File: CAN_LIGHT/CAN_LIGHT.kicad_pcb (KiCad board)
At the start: 2 copper layers, 135.5 x 115.4 mm, 94 parts, among them IC1 MSPM0C1103SDDFR, J1 Conn_ARM_SWD_TagConnect_TC2030

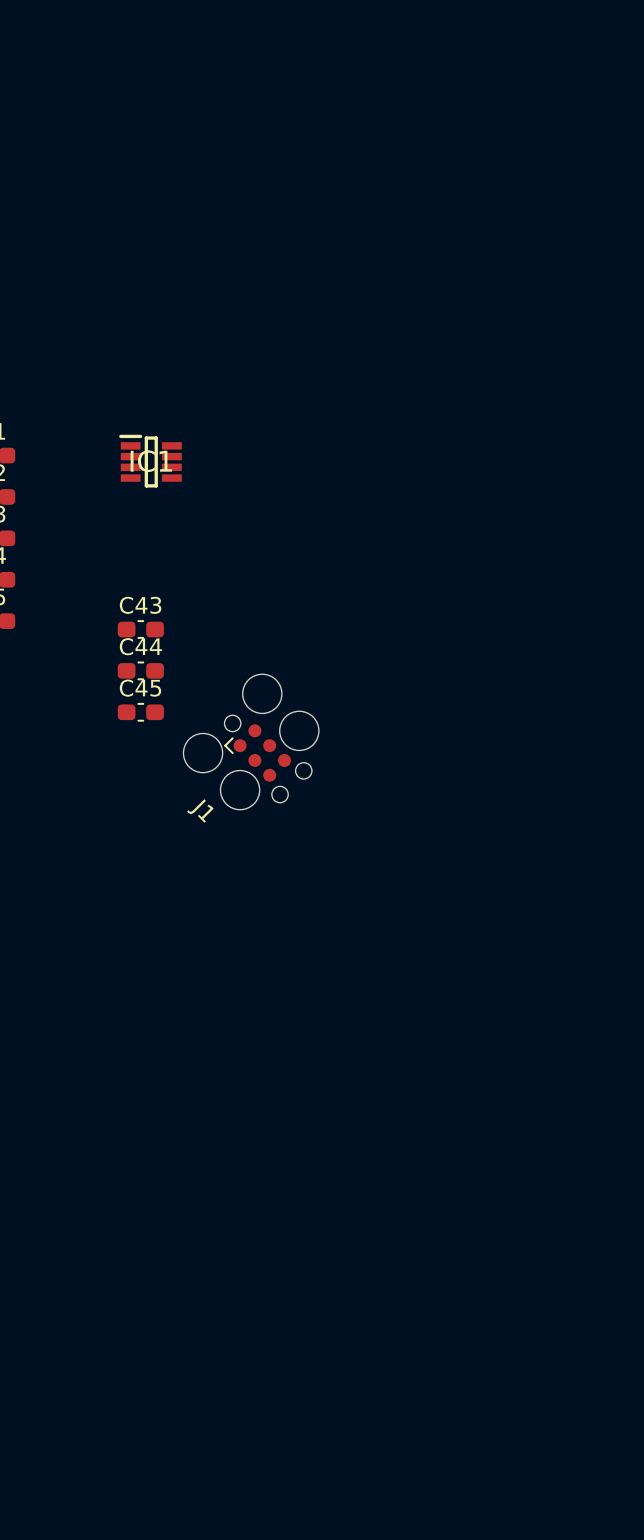
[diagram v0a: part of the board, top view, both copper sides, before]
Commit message: Export initial STEP file to print
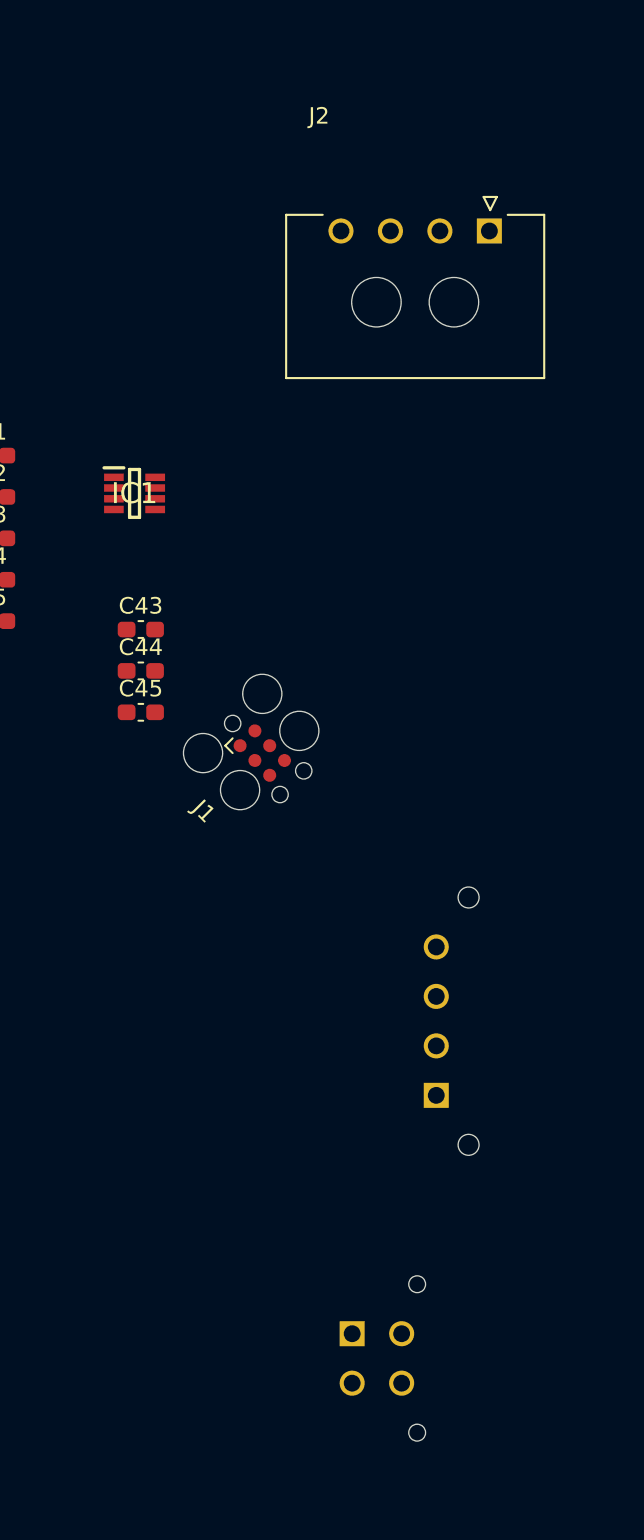
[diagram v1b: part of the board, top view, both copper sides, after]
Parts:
- added J2: 436500401, 436500401:MOLEX_436500401, F.Cu at (55.6, 42.4)
- added J3: 436500428, 436500428:CON_436500428_MOL, B.Cu at (52.3, 94.8)
- added J4: 430450428, 430450428:CON_430450428_MOL, B.Cu at (47.2, 109.3)
- moved IC1 2.16 mm to (34.0, 58.3)

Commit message: Add back side LEDs
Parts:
- removed IC1: MSPM0C1103SDDFR, MSPM0C1103SDDFR:SOT65P280X110-8N
- removed J4: 430450428, 430450428:CON_430450428_MOL
- added C46: 0.1uF, Capacitor_SMD:C_0603_1608Metric_Pad1.08x0.95mm_HandSolder, B.Cu at (230.2, 27.2)
- added C47: 0.1uF, Capacitor_SMD:C_0603_1608Metric_Pad1.08x0.95mm_HandSolder, B.Cu at (230.2, 29.7)
- added C48: 0.1uF, Capacitor_SMD:C_0603_1608Metric_Pad1.08x0.95mm_HandSolder, B.Cu at (230.2, 32.2)
- added C49: 0.1uF, Capacitor_SMD:C_0603_1608Metric_Pad1.08x0.95mm_HandSolder, B.Cu at (230.2, 34.7)
- added C50: 0.1uF, Capacitor_SMD:C_0603_1608Metric_Pad1.08x0.95mm_HandSolder, B.Cu at (230.2, 37.2)
- added C51: 0.1uF, Capacitor_SMD:C_0603_1608Metric_Pad1.08x0.95mm_HandSolder, B.Cu at (230.2, 39.7)
- added C52: 0.1uF, Capacitor_SMD:C_0603_1608Metric_Pad1.08x0.95mm_HandSolder, B.Cu at (230.2, 42.2)
- added C53: 0.1uF, Capacitor_SMD:C_0603_1608Metric_Pad1.08x0.95mm_HandSolder, B.Cu at (230.2, 44.7)
- added C54: 0.1uF, Capacitor_SMD:C_0603_1608Metric_Pad1.08x0.95mm_HandSolder, B.Cu at (230.2, 47.2)
- added C55: 0.1uF, Capacitor_SMD:C_0603_1608Metric_Pad1.08x0.95mm_HandSolder, B.Cu at (225.9, 27.2)
- added C56: 0.1uF, Capacitor_SMD:C_0603_1608Metric_Pad1.08x0.95mm_HandSolder, B.Cu at (225.9, 29.7)
- added C57: 0.1uF, Capacitor_SMD:C_0603_1608Metric_Pad1.08x0.95mm_HandSolder, B.Cu at (225.9, 32.2)
- added C58: 0.1uF, Capacitor_SMD:C_0603_1608Metric_Pad1.08x0.95mm_HandSolder, B.Cu at (225.9, 34.7)
- added C59: 0.1uF, Capacitor_SMD:C_0603_1608Metric_Pad1.08x0.95mm_HandSolder, B.Cu at (225.9, 37.2)
- added C60: 0.1uF, Capacitor_SMD:C_0603_1608Metric_Pad1.08x0.95mm_HandSolder, B.Cu at (225.9, 39.7)
- added C61: 0.1uF, Capacitor_SMD:C_0603_1608Metric_Pad1.08x0.95mm_HandSolder, B.Cu at (225.9, 42.2)
- added C62: 0.1uF, Capacitor_SMD:C_0603_1608Metric_Pad1.08x0.95mm_HandSolder, B.Cu at (225.9, 44.7)
- added C63: 0.1uF, Capacitor_SMD:C_0603_1608Metric_Pad1.08x0.95mm_HandSolder, B.Cu at (225.9, 47.2)
- added C64: 0.1uF, Capacitor_SMD:C_0603_1608Metric_Pad1.08x0.95mm_HandSolder, B.Cu at (221.5, 27.2)
- added C65: 0.1uF, Capacitor_SMD:C_0603_1608Metric_Pad1.08x0.95mm_HandSolder, B.Cu at (221.5, 29.7)
- added C66: 0.1uF, Capacitor_SMD:C_0603_1608Metric_Pad1.08x0.95mm_HandSolder, B.Cu at (221.5, 32.2)
- added C67: 0.1uF, Capacitor_SMD:C_0603_1608Metric_Pad1.08x0.95mm_HandSolder, B.Cu at (221.5, 34.7)
- added C68: 0.1uF, Capacitor_SMD:C_0603_1608Metric_Pad1.08x0.95mm_HandSolder, B.Cu at (221.5, 37.2)
- added C69: 0.1uF, Capacitor_SMD:C_0603_1608Metric_Pad1.08x0.95mm_HandSolder, B.Cu at (221.5, 39.7)
- added C70: 0.1uF, Capacitor_SMD:C_0603_1608Metric_Pad1.08x0.95mm_HandSolder, B.Cu at (221.5, 42.2)
- added C71: 0.1uF, Capacitor_SMD:C_0603_1608Metric_Pad1.08x0.95mm_HandSolder, B.Cu at (221.5, 44.7)
- added C72: 0.1uF, Capacitor_SMD:C_0603_1608Metric_Pad1.08x0.95mm_HandSolder, B.Cu at (221.5, 47.2)
- added C73: 0.1uF, Capacitor_SMD:C_0603_1608Metric_Pad1.08x0.95mm_HandSolder, B.Cu at (217.2, 27.2)
- added C74: 0.1uF, Capacitor_SMD:C_0603_1608Metric_Pad1.08x0.95mm_HandSolder, B.Cu at (217.2, 29.7)
- added C75: 0.1uF, Capacitor_SMD:C_0603_1608Metric_Pad1.08x0.95mm_HandSolder, B.Cu at (217.2, 32.2)
- added C76: 0.1uF, Capacitor_SMD:C_0603_1608Metric_Pad1.08x0.95mm_HandSolder, B.Cu at (217.2, 34.7)
- added C77: 0.1uF, Capacitor_SMD:C_0603_1608Metric_Pad1.08x0.95mm_HandSolder, B.Cu at (217.2, 37.2)
- added C78: 0.1uF, Capacitor_SMD:C_0603_1608Metric_Pad1.08x0.95mm_HandSolder, B.Cu at (217.2, 39.7)
- added C79: 0.1uF, Capacitor_SMD:C_0603_1608Metric_Pad1.08x0.95mm_HandSolder, B.Cu at (217.2, 42.2)
- added C80: 0.1uF, Capacitor_SMD:C_0603_1608Metric_Pad1.08x0.95mm_HandSolder, B.Cu at (217.2, 44.7)
- added C81: 0.1uF, Capacitor_SMD:C_0603_1608Metric_Pad1.08x0.95mm_HandSolder, B.Cu at (217.2, 47.2)
- added C82: 0.1uF, Capacitor_SMD:C_0603_1608Metric_Pad1.08x0.95mm_HandSolder, B.Cu at (212.8, 27.2)
- added C83: 0.1uF, Capacitor_SMD:C_0603_1608Metric_Pad1.08x0.95mm_HandSolder, B.Cu at (212.8, 29.7)
- added C84: 0.1uF, Capacitor_SMD:C_0603_1608Metric_Pad1.08x0.95mm_HandSolder, B.Cu at (212.8, 32.2)
- added C85: 0.1uF, Capacitor_SMD:C_0603_1608Metric_Pad1.08x0.95mm_HandSolder, B.Cu at (212.8, 34.7)
- added C86: 0.1uF, Capacitor_SMD:C_0603_1608Metric_Pad1.08x0.95mm_HandSolder, B.Cu at (212.8, 37.2)
- added C87: 0.1uF, Capacitor_SMD:C_0603_1608Metric_Pad1.08x0.95mm_HandSolder, B.Cu at (212.8, 39.7)
- added D43: ~, IN-PI4818QAS5R5G5BPW:INPI4818QAS5R5G5BPW, B.Cu at (270.6, 28.5)
- added D44: ~, IN-PI4818QAS5R5G5BPW:INPI4818QAS5R5G5BPW, B.Cu at (270.6, 33.4)
- added D45: ~, IN-PI4818QAS5R5G5BPW:INPI4818QAS5R5G5BPW, B.Cu at (270.6, 38.3)
- added D46: ~, IN-PI4818QAS5R5G5BPW:INPI4818QAS5R5G5BPW, B.Cu at (270.6, 43.2)
- added D47: ~, IN-PI4818QAS5R5G5BPW:INPI4818QAS5R5G5BPW, B.Cu at (270.6, 48.1)
- added D48: ~, IN-PI4818QAS5R5G5BPW:INPI4818QAS5R5G5BPW, B.Cu at (270.6, 53.0)
- added D49: ~, IN-PI4818QAS5R5G5BPW:INPI4818QAS5R5G5BPW, B.Cu at (270.6, 57.9)
- added D50: ~, IN-PI4818QAS5R5G5BPW:INPI4818QAS5R5G5BPW, B.Cu at (270.6, 62.8)
- added D51: ~, IN-PI4818QAS5R5G5BPW:INPI4818QAS5R5G5BPW, B.Cu at (270.6, 67.7)
- added D52: ~, IN-PI4818QAS5R5G5BPW:INPI4818QAS5R5G5BPW, B.Cu at (262.1, 28.5)
- added D53: ~, IN-PI4818QAS5R5G5BPW:INPI4818QAS5R5G5BPW, B.Cu at (262.1, 33.4)
- added D54: ~, IN-PI4818QAS5R5G5BPW:INPI4818QAS5R5G5BPW, B.Cu at (262.1, 38.3)
- added D55: ~, IN-PI4818QAS5R5G5BPW:INPI4818QAS5R5G5BPW, B.Cu at (262.1, 43.2)
- added D56: ~, IN-PI4818QAS5R5G5BPW:INPI4818QAS5R5G5BPW, B.Cu at (262.1, 48.1)
- added D57: ~, IN-PI4818QAS5R5G5BPW:INPI4818QAS5R5G5BPW, B.Cu at (262.1, 53.0)
- added D58: ~, IN-PI4818QAS5R5G5BPW:INPI4818QAS5R5G5BPW, B.Cu at (262.1, 57.9)
- added D59: ~, IN-PI4818QAS5R5G5BPW:INPI4818QAS5R5G5BPW, B.Cu at (262.1, 62.8)
- added D60: ~, IN-PI4818QAS5R5G5BPW:INPI4818QAS5R5G5BPW, B.Cu at (262.1, 67.7)
- added D61: ~, IN-PI4818QAS5R5G5BPW:INPI4818QAS5R5G5BPW, B.Cu at (253.6, 28.5)
- added D62: ~, IN-PI4818QAS5R5G5BPW:INPI4818QAS5R5G5BPW, B.Cu at (253.6, 33.4)
- added D63: ~, IN-PI4818QAS5R5G5BPW:INPI4818QAS5R5G5BPW, B.Cu at (253.6, 38.3)
- added D64: ~, IN-PI4818QAS5R5G5BPW:INPI4818QAS5R5G5BPW, B.Cu at (253.6, 43.2)
- added D65: ~, IN-PI4818QAS5R5G5BPW:INPI4818QAS5R5G5BPW, B.Cu at (253.6, 48.1)
- added D66: ~, IN-PI4818QAS5R5G5BPW:INPI4818QAS5R5G5BPW, B.Cu at (253.6, 53.0)
- added D67: ~, IN-PI4818QAS5R5G5BPW:INPI4818QAS5R5G5BPW, B.Cu at (253.6, 57.9)
- added D68: ~, IN-PI4818QAS5R5G5BPW:INPI4818QAS5R5G5BPW, B.Cu at (253.6, 62.8)
- added D69: ~, IN-PI4818QAS5R5G5BPW:INPI4818QAS5R5G5BPW, B.Cu at (253.6, 67.7)
- added D70: ~, IN-PI4818QAS5R5G5BPW:INPI4818QAS5R5G5BPW, B.Cu at (245.1, 28.5)
- added D71: ~, IN-PI4818QAS5R5G5BPW:INPI4818QAS5R5G5BPW, B.Cu at (245.1, 33.4)
- added D72: ~, IN-PI4818QAS5R5G5BPW:INPI4818QAS5R5G5BPW, B.Cu at (245.1, 38.3)
- added D73: ~, IN-PI4818QAS5R5G5BPW:INPI4818QAS5R5G5BPW, B.Cu at (245.1, 43.2)
- added D74: ~, IN-PI4818QAS5R5G5BPW:INPI4818QAS5R5G5BPW, B.Cu at (245.1, 48.1)
- added D75: ~, IN-PI4818QAS5R5G5BPW:INPI4818QAS5R5G5BPW, B.Cu at (245.1, 53.0)
- added D76: ~, IN-PI4818QAS5R5G5BPW:INPI4818QAS5R5G5BPW, B.Cu at (245.1, 57.9)
- added D77: ~, IN-PI4818QAS5R5G5BPW:INPI4818QAS5R5G5BPW, B.Cu at (245.1, 62.8)
- added D78: ~, IN-PI4818QAS5R5G5BPW:INPI4818QAS5R5G5BPW, B.Cu at (245.1, 67.7)
- added D79: ~, IN-PI4818QAS5R5G5BPW:INPI4818QAS5R5G5BPW, B.Cu at (236.6, 28.5)
- added D80: ~, IN-PI4818QAS5R5G5BPW:INPI4818QAS5R5G5BPW, B.Cu at (236.6, 33.4)
- added D81: ~, IN-PI4818QAS5R5G5BPW:INPI4818QAS5R5G5BPW, B.Cu at (236.6, 38.3)
- added D82: ~, IN-PI4818QAS5R5G5BPW:INPI4818QAS5R5G5BPW, B.Cu at (236.6, 43.2)
- added D83: ~, IN-PI4818QAS5R5G5BPW:INPI4818QAS5R5G5BPW, B.Cu at (236.6, 48.1)
- added D84: ~, IN-PI4818QAS5R5G5BPW:INPI4818QAS5R5G5BPW, B.Cu at (236.6, 53.0)
- added U1: MSPM0C1103SDDFR, MSPM0C1103SDDFR:SOT65P280X110-8N, B.Cu at (229.8, 50.7)
- J2: value 436500401 -> 436500428; footprint 436500401:MOLEX_436500401 -> 436500428:CON_436500428_MOL
- J3: value 436500428 -> 430450428; footprint 436500428:CON_436500428_MOL -> 430450428:CON_430450428_MOL
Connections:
- D42 pad 3: unconnected-(D42-DOUT-Pad3) -> Net-(D42-DOUT)

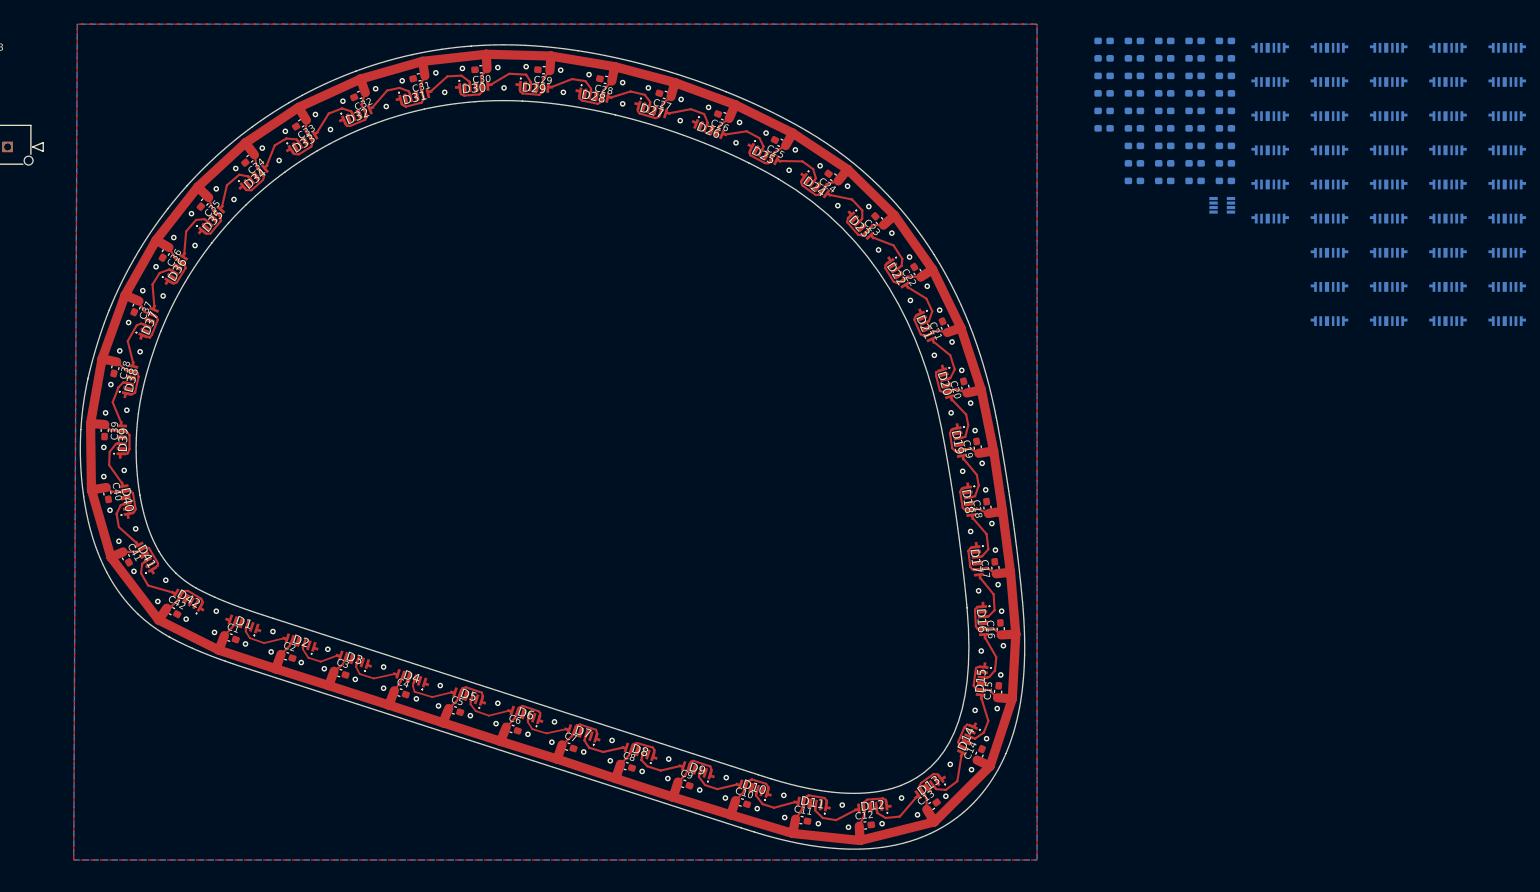
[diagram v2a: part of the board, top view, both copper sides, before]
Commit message: Roughly place backside LEDs
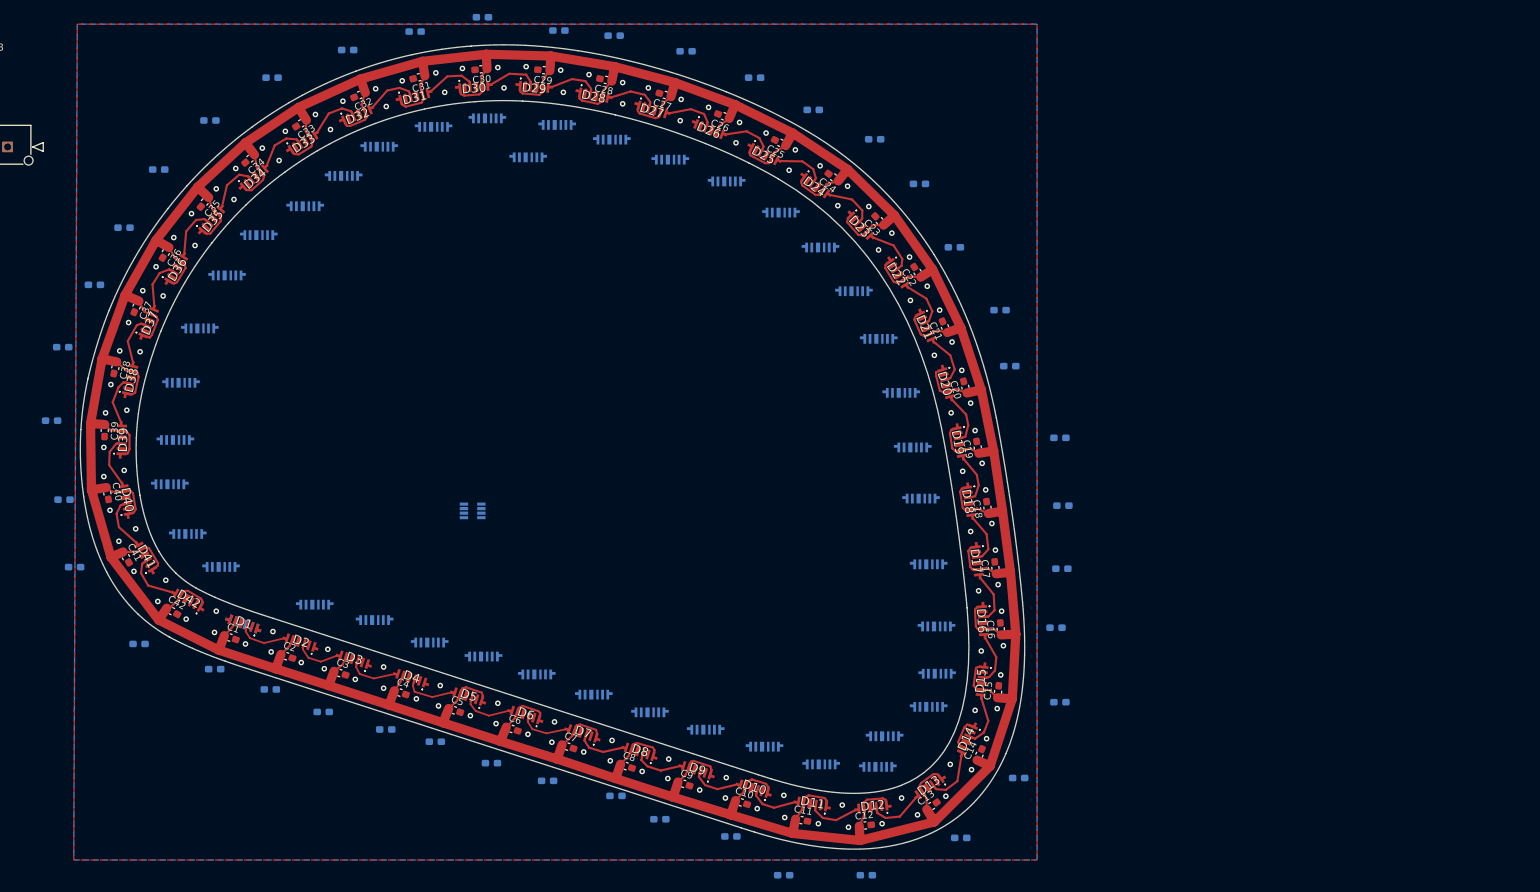
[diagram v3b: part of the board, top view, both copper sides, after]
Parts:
- moved D43 198.9 mm to (89.5, 110.5), turned to -19 degrees
- moved D44 186.8 mm to (99.6, 108.3)
- moved D45 177.8 mm to (108.2, 110.5)
- moved C46 170.7 mm to (85.2, 117.3), turned to 0 degrees
- moved D46 169.9 mm to (116.1, 113.8)
- moved D82 164.9 mm to (78.8, 91.1)
- moved C47 164.2 mm to (93.2, 120.2)
- moved D81 163.8 mm to (79.6, 84.7)
- moved D83 163.2 mm to (81.4, 98.2)
- moved D80 162.1 mm to (80.4, 76.5)
- moved D47 161.7 mm to (123.8, 115.8)
- moved C86 161.5 mm to (65.2, 102.6)
- moved C85 160.2 mm to (63.6, 93.0)
- moved C84 158.9 mm to (61.8, 81.6)
- moved D79 158.7 mm to (83.1, 68.7)
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
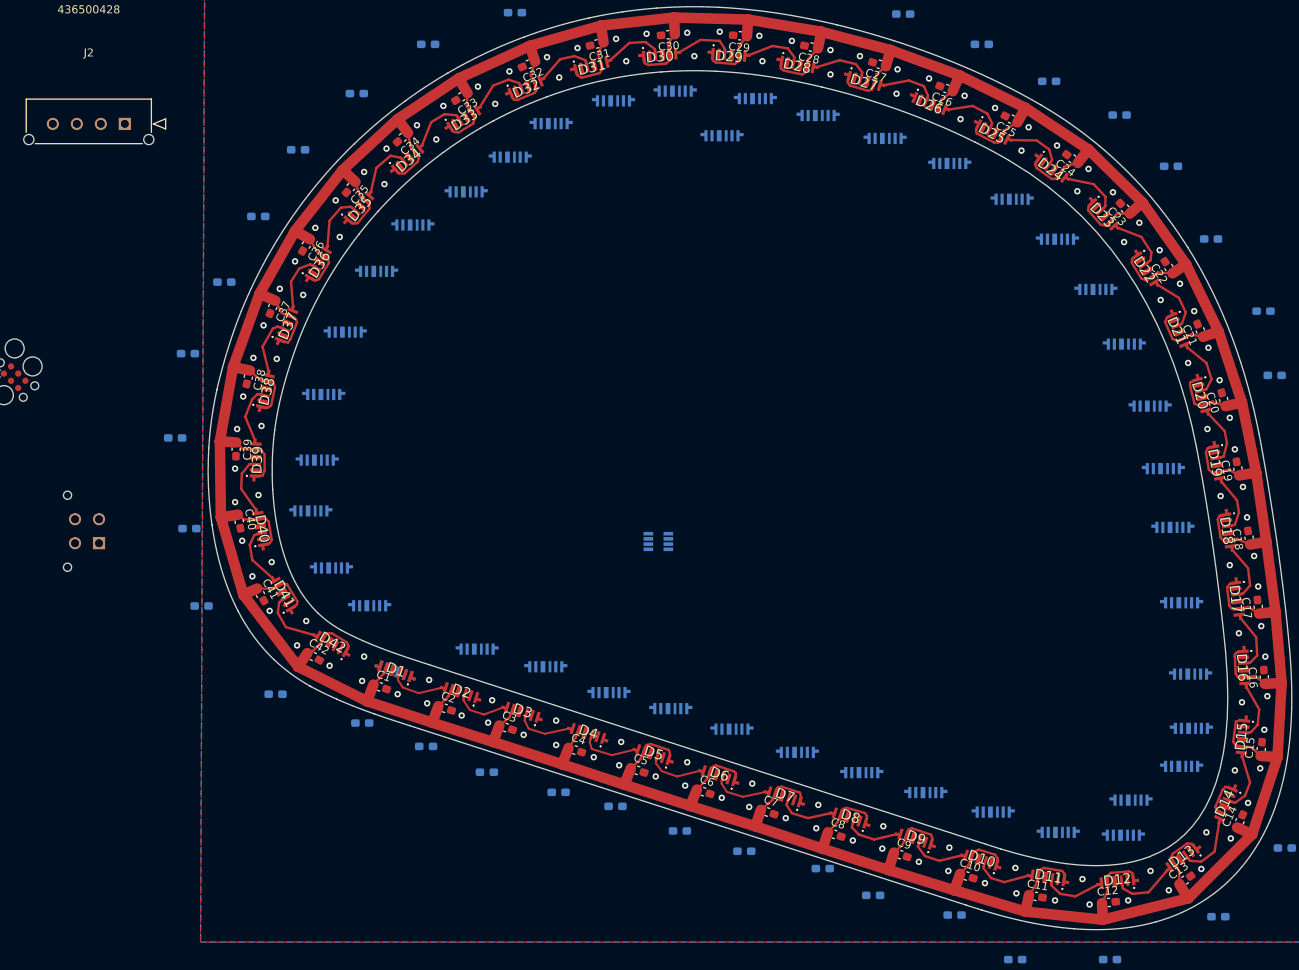
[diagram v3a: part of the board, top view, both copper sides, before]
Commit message: Set backside LEDs in place
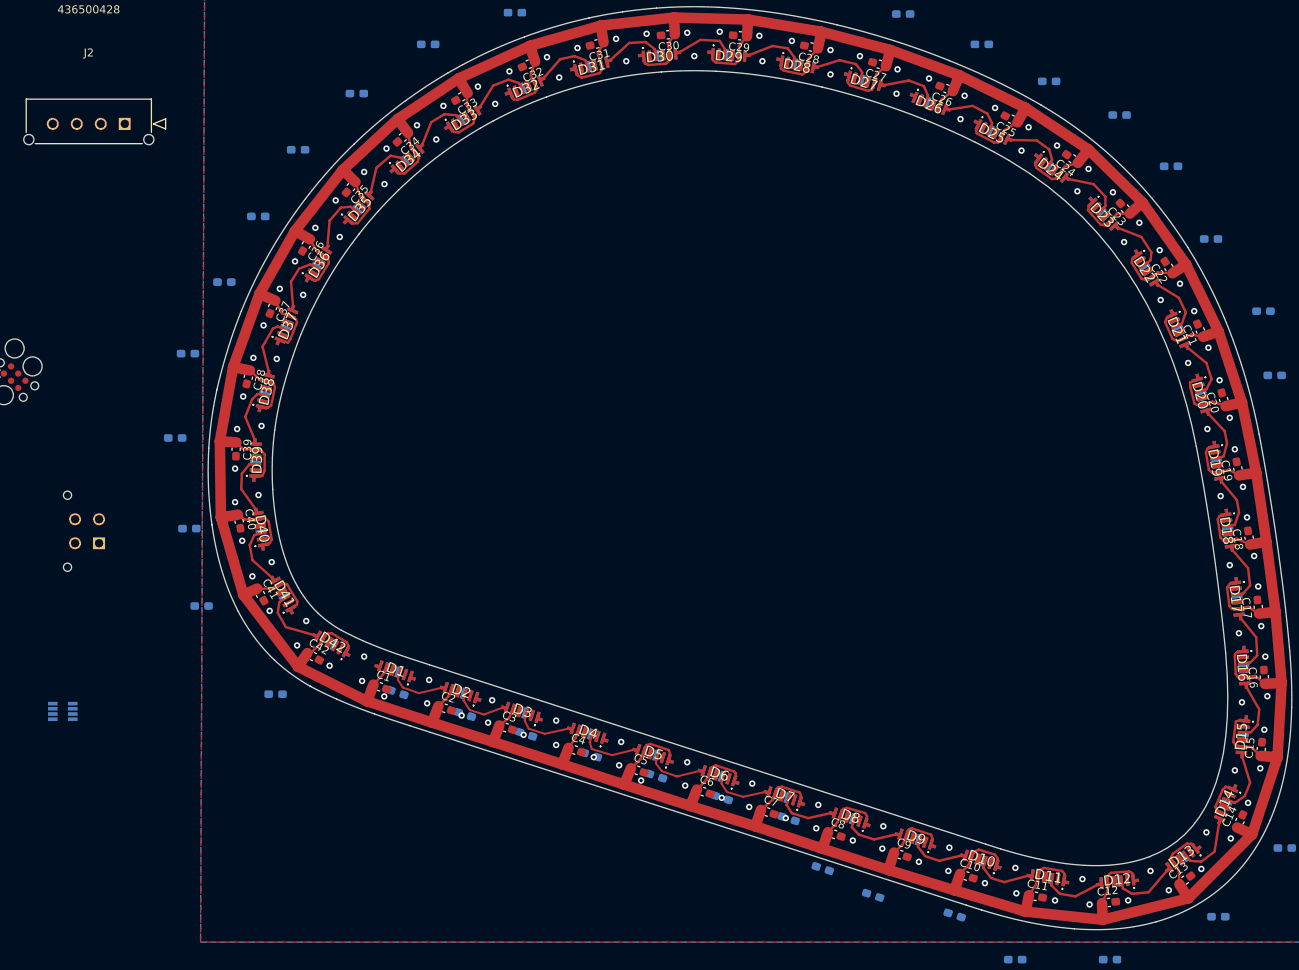
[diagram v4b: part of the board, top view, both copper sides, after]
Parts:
- moved U1 77.4 mm to (47.8, 115.8)
- moved D71 10.1 mm to (131.0, 34.1), turned to 175.5 degrees
- moved D55 9.17 mm to (187.6, 133.9), turned to 35.5 degrees
- moved D76 8.25 mm to (91.1, 47.0), turned to -139.75 degrees
- moved D75 7.47 mm to (98.1, 42.0), turned to -148.5 degrees
- moved D81 7.40 mm to (72.2, 84.4), turned to -91.6 degrees
- moved D69 7.18 mm to (147.9, 37.3), turned to 163.5 degrees
- moved D79 7.14 mm to (76.0, 67.7), turned to -113 degrees
- moved D78 7.11 mm to (80.0, 60.0), turned to -121.5 degrees
- moved D80 7.04 mm to (73.4, 75.9), turned to -103.75 degrees
- moved D68 7.02 mm to (156.1, 40.1), turned to 158.25 degrees
- moved D77 6.90 mm to (85.0, 53.1), turned to -130.75 degrees
- moved C52 6.87 mm to (138.5, 129.2), turned to 162 degrees
- moved C48 6.83 mm to (105.7, 118.7), turned to 162 degrees
- moved D56 6.81 mm to (192.9, 127.3), turned to 66 degrees
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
